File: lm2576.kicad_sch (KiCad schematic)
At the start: 8 parts, among them J5 DC_IN, U9 LM2576HVS-3.3

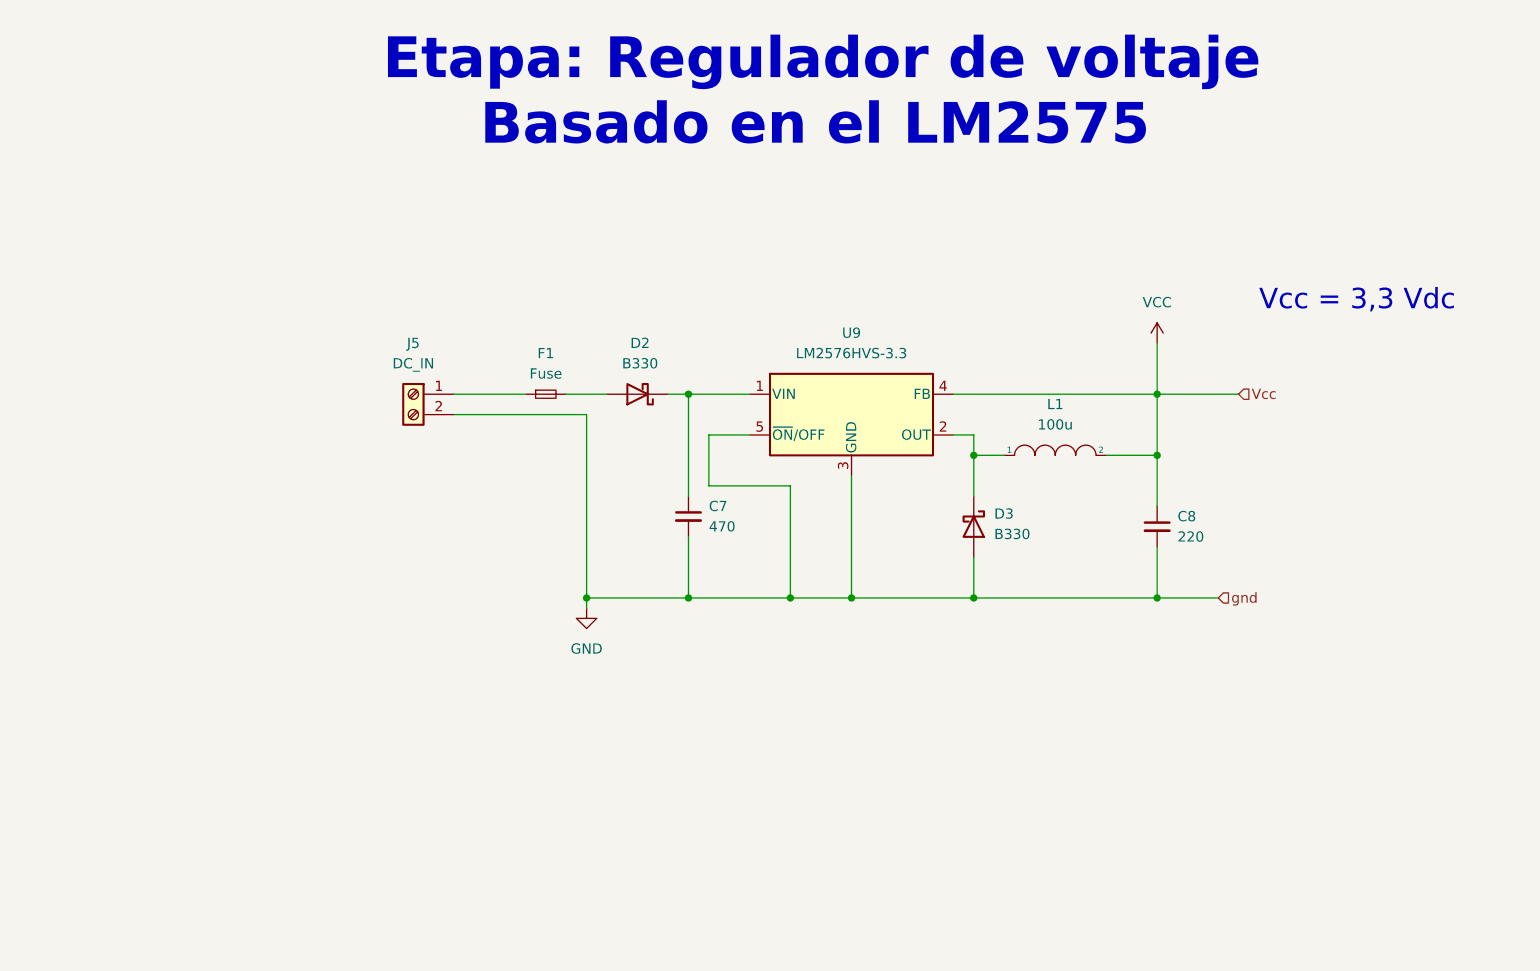
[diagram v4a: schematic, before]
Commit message: input/output separadas
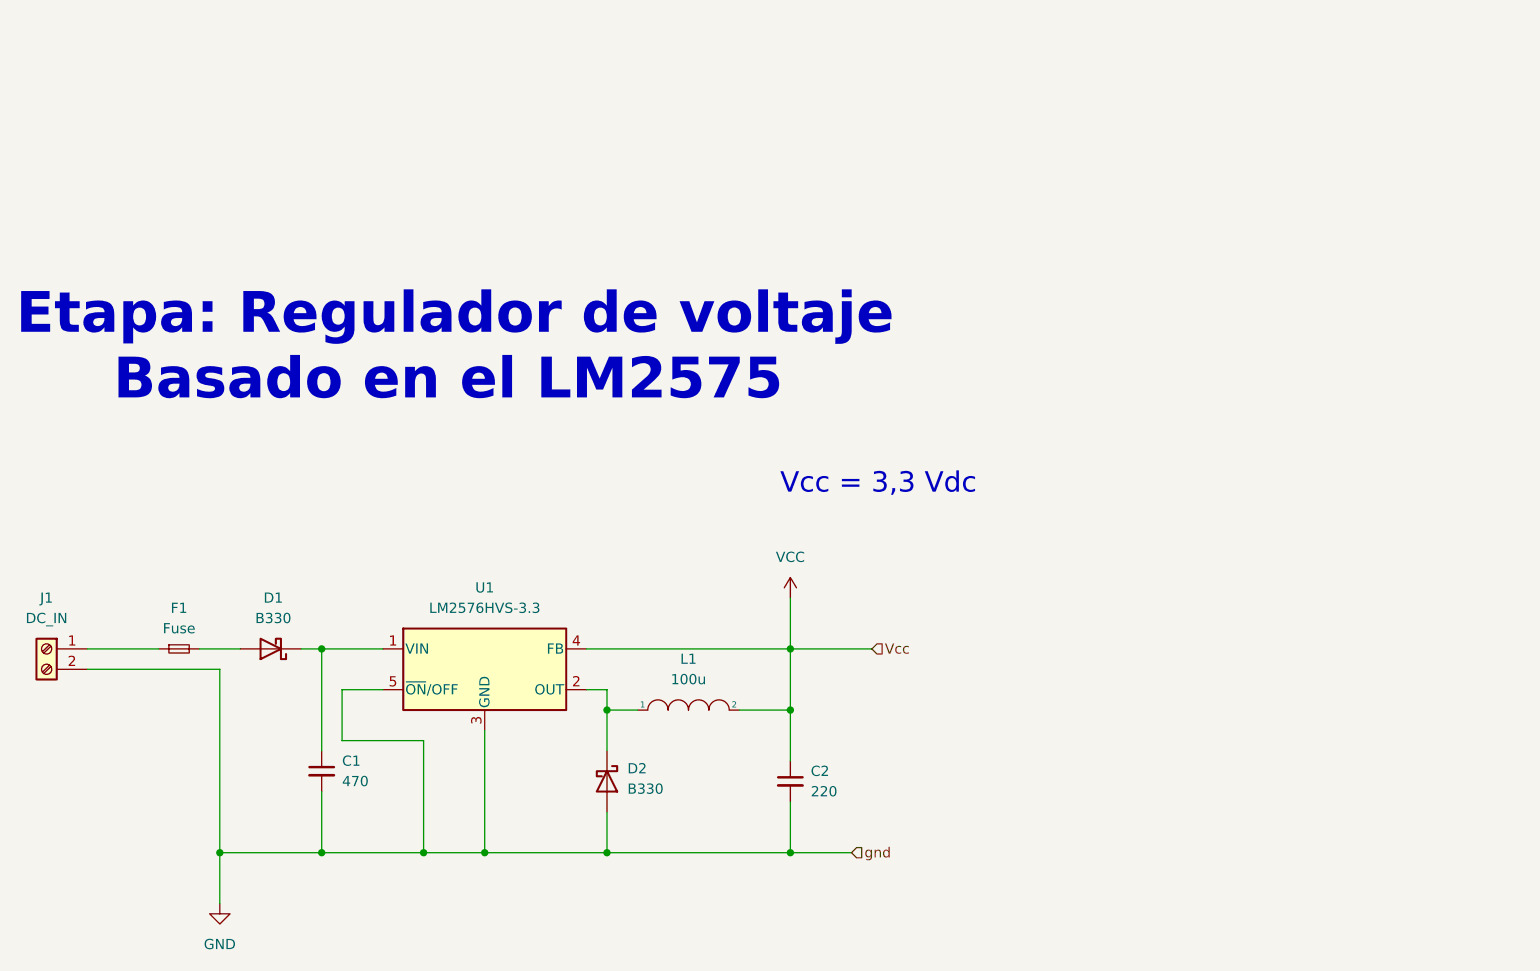
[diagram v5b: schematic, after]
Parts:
- renumbered C7 to C1, C8 to C2, D2 to D1, D3 to D2, J5 to J1, U9 to U1
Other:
- moved on the sheet: C1, C2, D1, D2, F1, J1, L1, U1

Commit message: add
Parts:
- renumbered C1 to C2, C2 to C3, D1 to D2, D2 to D3, J1 to J5, U1 to U2
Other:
- moved on the sheet: U2
